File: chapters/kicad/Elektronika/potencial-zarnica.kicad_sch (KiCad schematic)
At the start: 6 parts

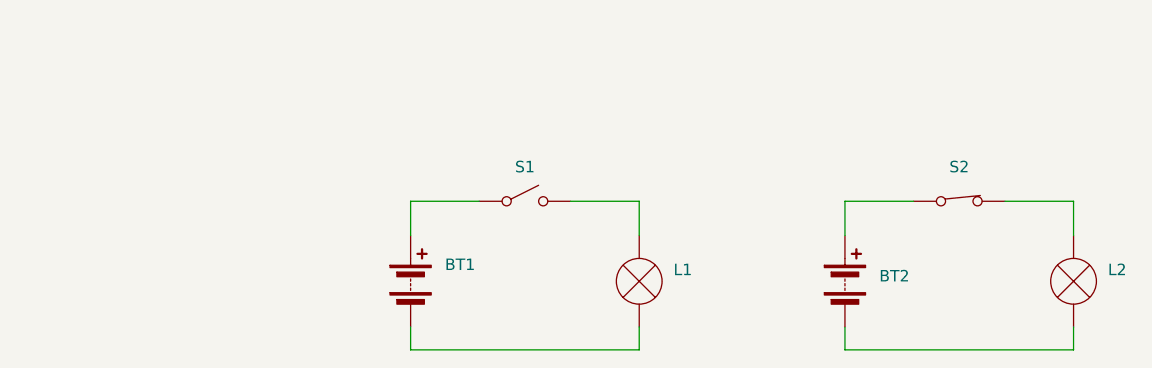
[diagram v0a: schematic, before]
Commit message: odstranjene omembe o prenosu energije z nabolji
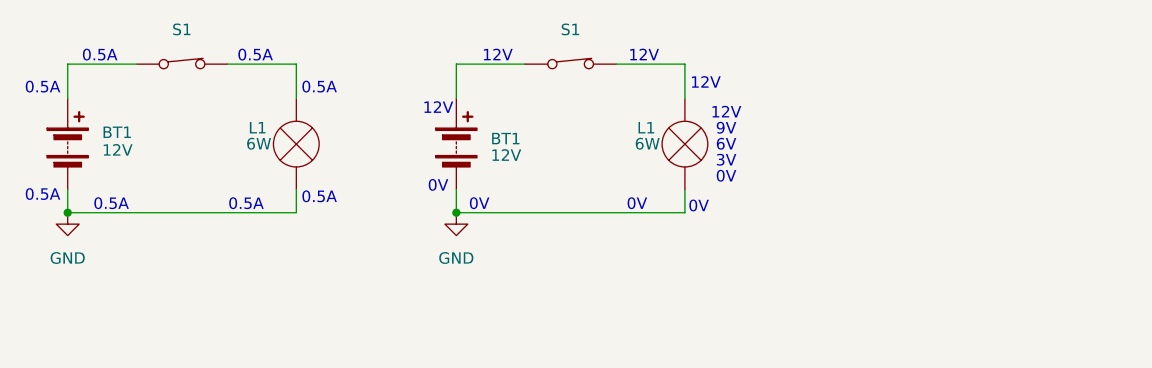
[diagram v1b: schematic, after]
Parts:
- removed BT1, BT2: Battery, symbol Device:Battery
- removed L1, L2: Lamp, symbol Device:Lamp
- removed S: S1, symbol Switch:SW_DPST_x2
- removed S1: S2, symbol Switch:SW_DPST_x2
- added BT1 (x2): 12V, symbol Device:Battery
- added L1 (x2): 6W, symbol Device:Lamp
- added S2, S3: S1, symbol Switch:SW_DPST_x2
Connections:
- new net: BT1.1 (+), S3.1 (A)
- new net: L1.2 (+), S3.2 (B)
- new net: L1.2 (+), S2.2 (B)
- new net: BT1.1 (+), S2.1 (A)
- new net GND: BT1.2 (-), BT1.2 (-), L1.1 (-), L1.1 (-)
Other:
- note added: "0.5A"
- note added: "0V"
- note added: "12V"
- note added: "3V"
- note added: "6V"
- note added: "9V"
